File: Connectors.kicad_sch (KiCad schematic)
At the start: 4 parts

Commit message: complete footprint association
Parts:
- J1: renamed from J?; value Conn_01x04 -> Serial; footprint (none) -> Connector_PinSocket_2.54mm:PinSocket_1x04_P2.54mm_Vertical
- J2: renamed from J?; value Conn_01x09 -> Digital Pins; footprint (none) -> Connector_PinSocket_2.54mm:PinSocket_1x09_P2.54mm_Vertical
- J3: renamed from J?; value Conn_01x04 -> I2C; footprint (none) -> Connector_PinSocket_2.54mm:PinSocket_1x04_P2.54mm_Vertical
- J4: renamed from J?; value Conn_02x03_Odd_Even -> ICSP; footprint (none) -> Connector_PinSocket_2.54mm:PinSocket_2x03_P2.54mm_Vertical
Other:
- moved on the sheet: J1, J2, J3, J4
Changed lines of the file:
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@@
     (comment 1 "Designed by Yogesh")
   )
-  (symbol (lib_id "Connector_Generic:Conn_01x04") (at 152.4 60.96 0) (unit 1)
+  (symbol (lib_id "Connector_Generic:Conn_01x04") (at 82.55 63.5 0) (unit 1)
     (in_bom yes) (on_board yes) (fields_autoplaced)
-    (property "Reference" "J?" (id 0) (at 154.94 60.9599 0)
+    (property "Reference" "J1" (id 0) (at 85.09 63.4999 0)
       (effects (font (size 1.27 1.27)) (justify left))
     )
-    (property "Value" "Conn_01x04" (id 1) (at 154.94 63.4999 0)
+    (property "Value" "Serial" (id 1) (at 85.09 66.0399 0)
       (effects (font (size 1.27 1.27)) (justify left))
     )
-    (property "Footprint" "" (id 2) (at 152.4 60.96 0)
+    (property "Footprint" "Connector_PinSocket_2.54mm:PinSocket_1x04_P2.54mm_Vertical" (id 2) (at 82.55 63.5 0)
       (effects (font (size 1.27 1.27)) hide)
     )
-    (property "Datasheet" "~" (id 3) (at 152.4 60.96 0)
+    (property "Datasheet" "~" (id 3) (at 82.55 63.5 0)
       (effects (font (size 1.27 1.27)) hide)
     )
@@
     (pin "4")
   )
-  (symbol (lib_id "Connector_Generic:Conn_01x04") (at 154.94 102.87 0) (unit 1)
+  (symbol (lib_id "Connector_Generic:Conn_01x04") (at 113.03 62.23 0) (unit 1)
     (in_bom yes) (on_board yes) (fields_autoplaced)
-    (property "Reference" "J?" (id 0) (at 157.48 102.8699 0)
+    (property "Reference" "J3" (id 0) (at 115.57 62.2299 0)
       (effects (font (size 1.27 1.27)) (justify left))
     )
-    (property "Value" "Conn_01x04" (id 1) (at 157.48 105.4099 0)
+    (property "Value" "I2C" (id 1) (at 115.57 64.7699 0)
       (effects (font (size 1.27 1.27)) (justify left))
     )
-    (property "Footprint" "" (id 2) (at 154.94 102.87 0)
+    (property "Footprint" "Connector_PinSocket_2.54mm:PinSocket_1x04_P2.54mm_Vertical" (id 2) (at 113.03 62.23 0)
       (effects (font (size 1.27 1.27)) hide)
     )
-    (property "Datasheet" "~" (id 3) (at 154.94 102.87 0)
+    (property "Datasheet" "~" (id 3) (at 113.03 62.23 0)
       (effects (font (size 1.27 1.27)) hide)
     )
@@
     (pin "4")
   )
-  (symbol (lib_id "Connector_Generic:Conn_02x03_Odd_Even") (at 88.9 107.95 0) (unit 1)
+  (symbol (lib_id "Connector_Generic:Conn_02x03_Odd_Even") (at 114.3 109.22 0) (unit 1)
     (in_bom yes) (on_board yes) (fields_autoplaced)
-    (property "Reference" "J?" (id 0) (at 90.17 99.06 0))
-    (property "Value" "Conn_02x03_Odd_Even" (id 1) (at 90.17 101.6 0))
-    (property "Footprint" "" (id 2) (at 88.9 107.95 0)
+    (property "Reference" "J4" (id 0) (at 115.57 100.33 0))
+    (property "Value" "ICSP" (id 1) (at 115.57 102.87 0))
+    (property "Footprint" "Connector_PinSocket_2.54mm:PinSocket_2x03_P2.54mm_Vertical" (id 2) (at 114.3 109.22 0)
       (effects (font (size 1.27 1.27)) hide)
     )
-    (property "Datasheet" "~" (id 3) (at 88.9 107.95 0)
+    (property "Datasheet" "~" (id 3) (at 114.3 109.22 0)
       (effects (font (size 1.27 1.27)) hide)
     )
@@
     (pin "6")
   )
-  (symbol (lib_id "Connector_Generic:Conn_01x09") (at 88.9 71.12 0) (unit 1)
+  (symbol (lib_id "Connector_Generic:Conn_01x09") (at 82.55 110.49 0) (unit 1)
     (in_bom yes) (on_board yes) (fields_autoplaced)
-    (property "Reference" "J?" (id 0) (at 91.44 69.8499 0)
+    (property "Reference" "J2" (id 0) (at 85.09 109.2199 0)
       (effects (font (size 1.27 1.27)) (justify left))
     )
-    (property "Value" "Conn_01x09" (id 1) (at 91.44 72.3899 0)
+    (property "Value" "Digital Pins" (id 1) (at 85.09 111.7599 0)
       (effects (font (size 1.27 1.27)) (justify left))
     )
-    (property "Footprint" "" (id 2) (at 88.9 71.12 0)
+    (property "Footprint" "Connector_PinSocket_2.54mm:PinSocket_1x09_P2.54mm_Vertical" (id 2) (at 82.55 110.49 0)
       (effects (font (size 1.27 1.27)) hide)
     )
-    (property "Datasheet" "~" (id 3) (at 88.9 71.12 0)
+    (property "Datasheet" "~" (id 3) (at 82.55 110.49 0)
       (effects (font (size 1.27 1.27)) hide)
     )

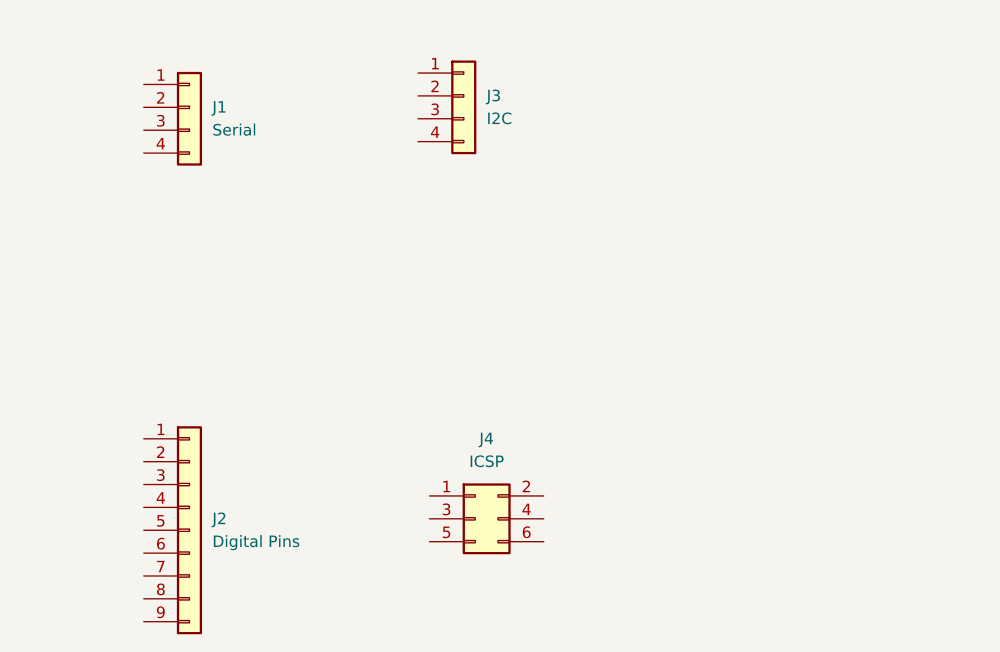
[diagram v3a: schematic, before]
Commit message: complete wiring in the root sheet
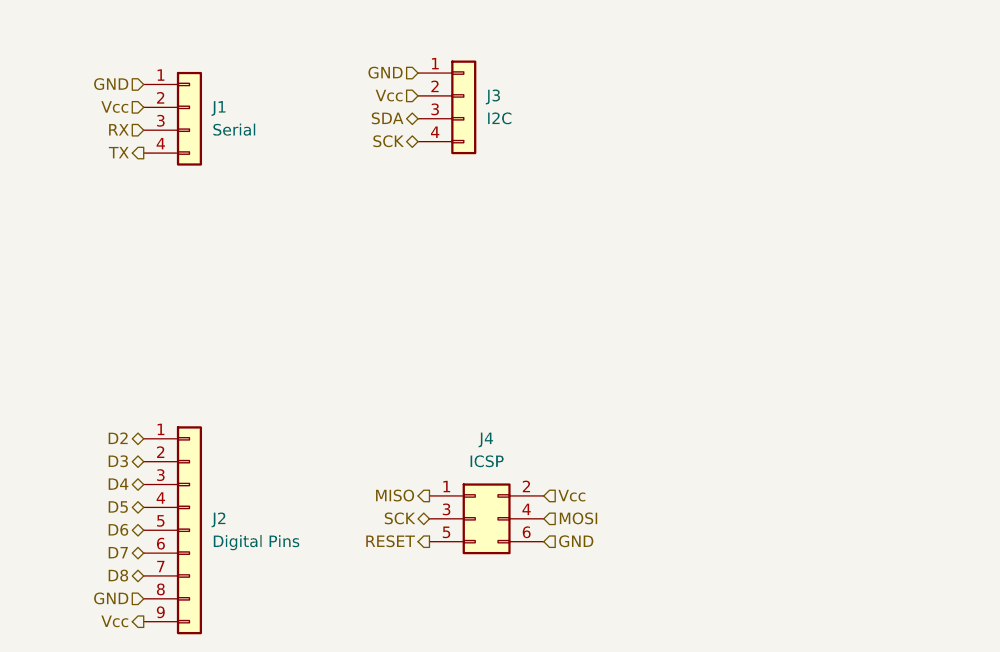
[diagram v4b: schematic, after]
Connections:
- net GND: now reaches J1.1 (Pin_1)
- net GND: now also J2.8 (Pin_8), J3.1 (Pin_1), J4.6 (Pin_6)
- net Vcc: now reaches J1.2 (Pin_2)
- net Vcc: now also J2.9 (Pin_9), J3.2 (Pin_2), J4.2 (Pin_2)
- net RX: now reaches J1.3 (Pin_3)
- net TX: now reaches J1.4 (Pin_4)
- net SDA: now reaches J3.3 (Pin_3)
- net SCK: now reaches J3.4 (Pin_4)
- net SCK: now also J4.3 (Pin_3)
- net MISO: now reaches J4.1 (Pin_1)
- net MOSI: now reaches J4.4 (Pin_4)
- net RESET: now reaches J4.5 (Pin_5)
- net D2: now reaches J2.1 (Pin_1)
- net D3: now reaches J2.2 (Pin_2)
- net D4: now reaches J2.3 (Pin_3)
- net D5: now reaches J2.4 (Pin_4)
- net D6: now reaches J2.5 (Pin_5)
- net D7: now reaches J2.6 (Pin_6)
- net D8: now reaches J2.7 (Pin_7)
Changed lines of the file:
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@@
     (comment 1 "Designed by Yogesh")
+  )
+  (hierarchical_label "TX" (shape output) (at 77.47 68.58 180)
+    (effects (font (size 1.27 1.27)) (justify right))
+  )
+  (hierarchical_label "Vcc" (shape input) (at 77.47 63.5 180)
+    (effects (font (size 1.27 1.27)) (justify right))
+  )
+  (hierarchical_label "RX" (shape input) (at 77.47 66.04 180)
+    (effects (font (size 1.27 1.27)) (justify right))
+  )
+  (hierarchical_label "GND" (shape input) (at 107.95 59.69 180)
+    (effects (font (size 1.27 1.27)) (justify right))
+  )
+  (hierarchical_label "SCK" (shape bidirectional) (at 109.22 109.22 180)
+    (effects (font (size 1.27 1.27)) (justify right))
+  )
+  (hierarchical_label "MOSI" (shape input) (at 121.92 109.22 0)
+    (effects (font (size 1.27 1.27)) (justify left))
+  )
+  (hierarchical_label "GND" (shape input) (at 77.47 60.96 180)
+    (effects (font (size 1.27 1.27)) (justify right))
+  )
+  (hierarchical_label "D5" (shape bidirectional) (at 77.47 107.95 180)
+    (effects (font (size 1.27 1.27)) (justify right))
+  )
+  (hierarchical_label "D7" (shape bidirectional) (at 77.47 113.03 180)
+    (effects (font (size 1.27 1.27)) (justify right))
+  )
+  (hierarchical_label "RESET" (shape output) (at 109.22 111.76 180)
+    (effects (font (size 1.27 1.27)) (justify right))
+  )
+  (hierarchical_label "GND" (shape input) (at 77.47 118.11 180)
+    (effects (font (size 1.27 1.27)) (justify right))
+  )
+  (hierarchical_label "Vcc" (shape output) (at 77.47 120.65 180)
+    (effects (font (size 1.27 1.27)) (justify right))
+  )
+  (hierarchical_label "D3" (shape bidirectional) (at 77.47 102.87 180)
+    (effects (font (size 1.27 1.27)) (justify right))
+  )
+  (hierarchical_label "GND" (shape input) (at 121.92 111.76 0)
+    (effects (font (size 1.27 1.27)) (justify left))
+  )
+  (hierarchical_label "Vcc" (shape input) (at 107.95 62.23 180)
+    (effects (font (size 1.27 1.27)) (justify right))
+  )
+  (hierarchical_label "SCK" (shape bidirectional) (at 107.95 67.31 180)
+    (effects (font (size 1.27 1.27)) (justify right))
+  )
+  (hierarchical_label "D2" (shape bidirectional) (at 77.47 100.33 180)
+    (effects (font (size 1.27 1.27)) (justify right))
+  )
+  (hierarchical_label "D4" (shape bidirectional) (at 77.47 105.41 180)
+    (effects (font (size 1.27 1.27)) (justify right))
+  )
+  (hierarchical_label "MISO" (shape output) (at 109.22 106.68 180)
+    (effects (font (size 1.27 1.27)) (justify right))
+  )
+  (hierarchical_label "D8" (shape bidirectional) (at 77.47 115.57 180)
+    (effects (font (size 1.27 1.27)) (justify right))
+  )
+  (hierarchical_label "SDA" (shape bidirectional) (at 107.95 64.77 180)
+    (effects (font (size 1.27 1.27)) (justify right))
+  )
+  (hierarchical_label "Vcc" (shape input) (at 121.92 106.68 0)
+    (effects (font (size 1.27 1.27)) (justify left))
+  )
+  (hierarchical_label "D6" (shape bidirectional) (at 77.47 110.49 180)
+    (effects (font (size 1.27 1.27)) (justify right))
   )
   (symbol (lib_id "Connector_Generic:Conn_01x04") (at 82.55 63.5 0) (unit 1)

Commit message: add functional block description
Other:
- note added: "N4-Serial Connector"
- note added: "N5-I2C Connector"
- note added: "N6-GPIO Connector"
- note added: "N7-SPI Connector"
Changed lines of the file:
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@@
     (comment 1 "Designed by Yogesh")
+  )
+  (text "N4-Serial Connector" (at 87.63 57.15 180)
+    (effects (font (size 1.27 1.27)) (justify right bottom))
+  )
+  (text "N6-GPIO Connector" (at 90.17 96.52 180)
+    (effects (font (size 1.27 1.27)) (justify right bottom))
+  )
+  (text "N5-I2C Connector\n" (at 115.57 55.88 180)
+    (effects (font (size 1.27 1.27)) (justify right bottom))
+  )
+  (text "N7-SPI Connector\n" (at 120.65 97.79 180)
+    (effects (font (size 1.27 1.27)) (justify right bottom))
   )
   (hierarchical_label "TX" (shape output) (at 77.47 68.58 180)
